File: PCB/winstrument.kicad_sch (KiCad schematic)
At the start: 94 parts, among them J1 Conn_01x05_Pin, J2 ICSP, J3 RS422, J4 Conn_01x08_Pin, J5 Conn_02x04_Odd_Even, J6 Conn_01x03_Pin, J7 Conn_01x02_Pin, Q1 2N7002, Q2 2N7002, Q3 2N7002, U1 STM32L432KCUx, U10 TLV9061xDBV, U11 TCMT1100, U12 TCMT1100, U2 TCAN337, U3 TPS5430DDA, U4 ADM3488ExR, U5 TLV75533PDBV, U6 NCP662SQ50, U7 TXB0104D, U8 TLV9061xDBV, U9 TPS27SA08CPWPR

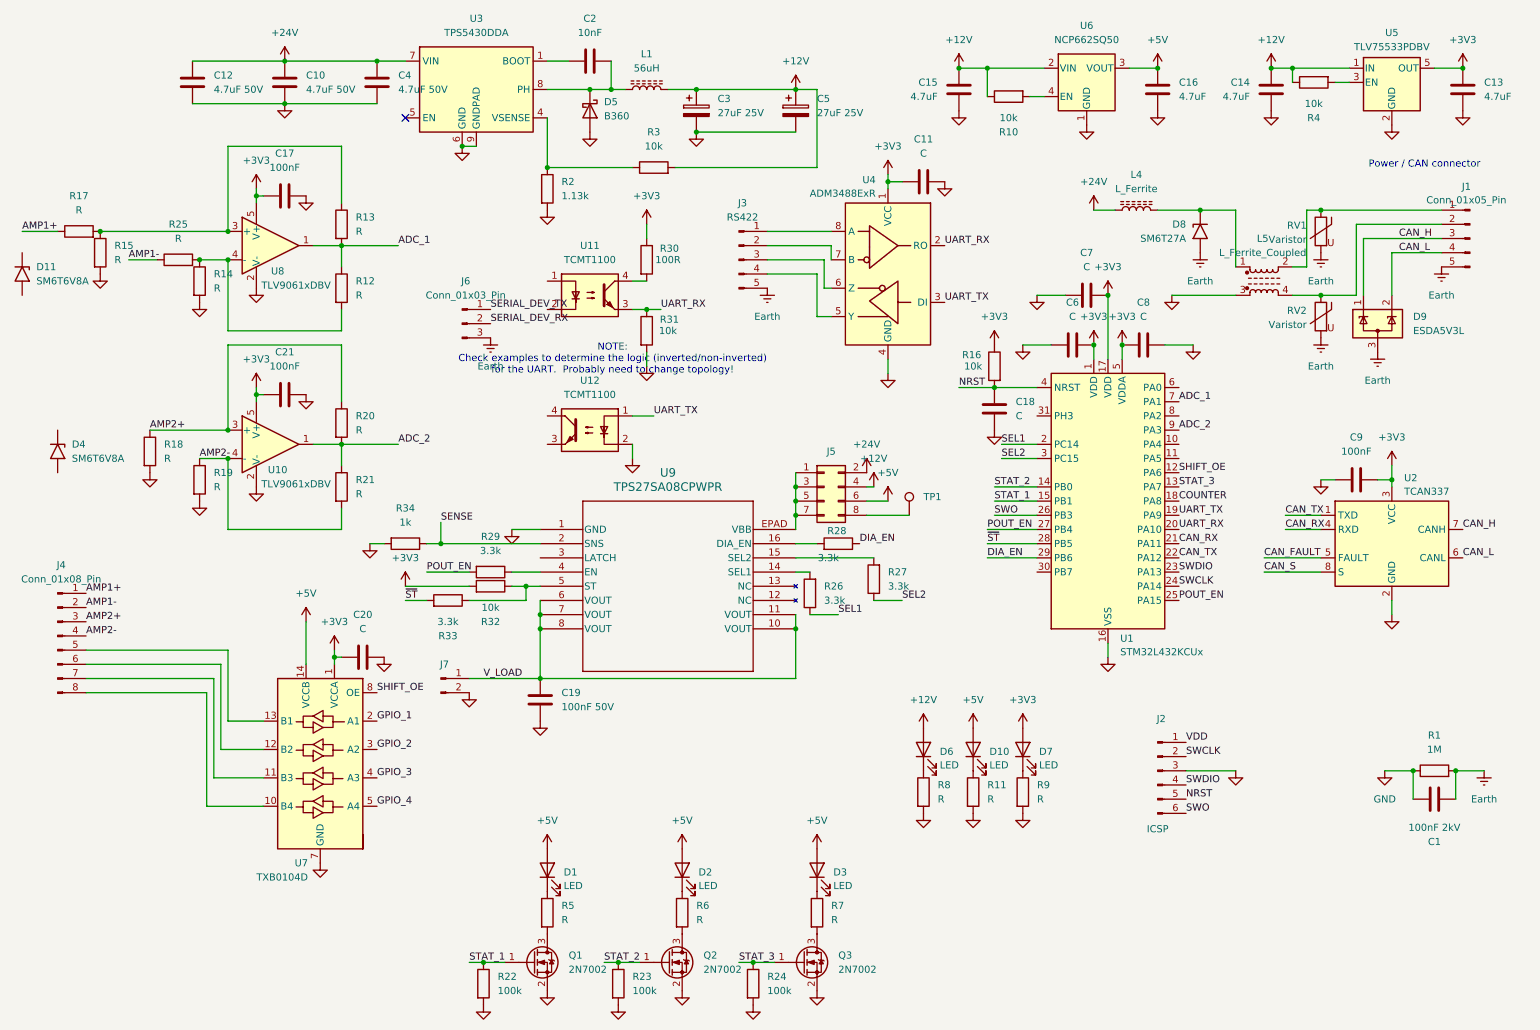
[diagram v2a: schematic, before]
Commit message: schematic capture and part specification mostly complete.  Still some uncertainty on the power common mode filter choke, could possibly go with a through-hole part on a toroid.  At least one footprint that requires creating or correcting, otherwise PCB is started.  No enclosure specified yet.
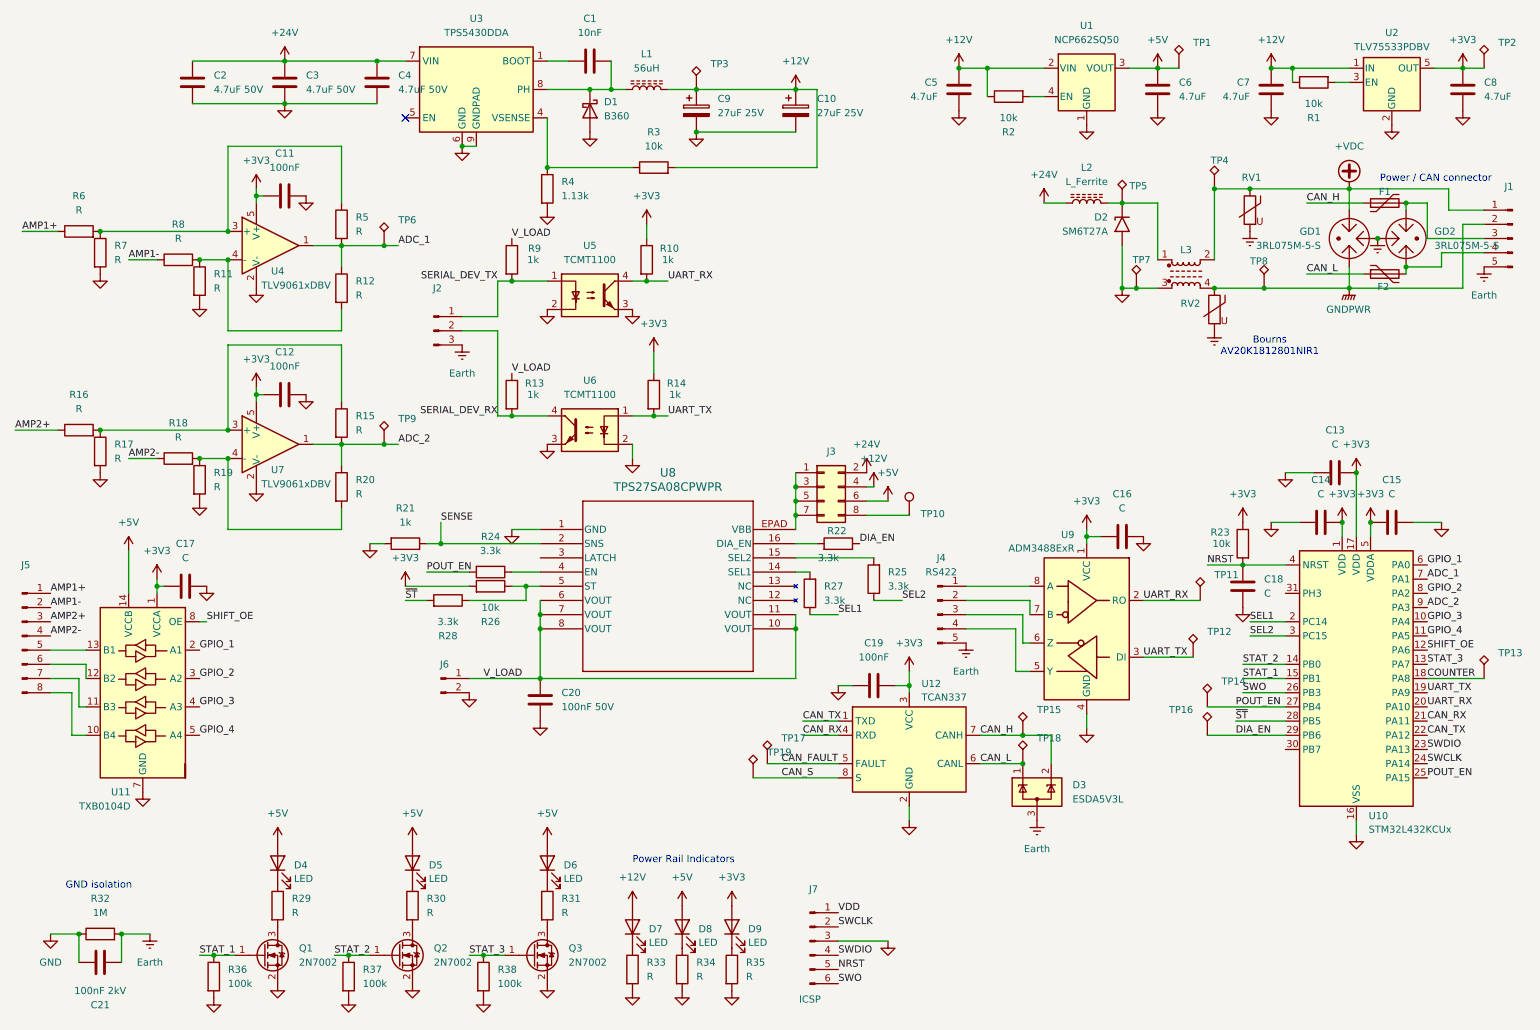
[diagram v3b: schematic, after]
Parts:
- removed D11, D4: SM6T6V8A, Diode_SMD:D_SMB, symbol Diode:SM6T6V8A
- removed J6: Conn_01x03_Pin, symbol Connector:Conn_01x03_Pin
- removed R31: 10k, symbol Device:R
- added F1, F2: TBU-CA-025-200-WH, Fuse:Fuse_Bourns_TBU-CA, symbol Power_Protection:TBU-CA-025-200-WH
- added GD1, GD2: 3RL075M-5-S, footprints:3R-5-S, symbol Device:GDT_3Pin
- added J2: Conn_01x03_Pin, Connector_Molex:Molex_KK-254_AE-6410-03A_1x03_P2.54mm_Vertical, symbol Connector:Conn_01x03_Pin
- added R13, R14, R9: 1k, Resistor_SMD:R_0603_1608Metric_Pad0.98x0.95mm_HandSolder, symbol Device:R
- added R16, R18: R, Resistor_SMD:R_0603_1608Metric_Pad0.98x0.95mm_HandSolder, symbol Device:R
- added TP1, TP11, TP12, TP13, TP14, TP15, TP16, TP17, TP18, TP19, TP2, TP3, TP4, TP5, TP6, TP7, TP8, TP9: TestPoint_Alt, TestPoint:TestPoint_Keystone_5019_Minature, symbol Connector:TestPoint_Alt
- C1: renamed from C2; footprint (none) -> Capacitor_SMD:C_0603_1608Metric_Pad1.08x0.95mm_HandSolder
- C10: renamed from C5; footprint (none) -> Capacitor_SMD:C_1808_4520Metric
- C11: renamed from C17; footprint (none) -> Capacitor_SMD:C_0603_1608Metric_Pad1.08x0.95mm_HandSolder
- C12: renamed from C21; footprint (none) -> Capacitor_SMD:C_0603_1608Metric_Pad1.08x0.95mm_HandSolder
- C13: renamed from C7; footprint (none) -> Capacitor_SMD:C_0603_1608Metric_Pad1.08x0.95mm_HandSolder
- C14: renamed from C6; footprint (none) -> Capacitor_SMD:C_0603_1608Metric_Pad1.08x0.95mm_HandSolder
- C15: renamed from C8; footprint (none) -> Capacitor_SMD:C_0603_1608Metric_Pad1.08x0.95mm_HandSolder
- C16: renamed from C11; footprint (none) -> Capacitor_SMD:C_0603_1608Metric_Pad1.08x0.95mm_HandSolder
- C17: renamed from C20; footprint (none) -> Capacitor_SMD:C_0603_1608Metric_Pad1.08x0.95mm_HandSolder
- C18: footprint (none) -> Capacitor_SMD:C_0603_1608Metric_Pad1.08x0.95mm_HandSolder
- C19: renamed from C9; footprint (none) -> Capacitor_SMD:C_0603_1608Metric_Pad1.08x0.95mm_HandSolder
- C2: renamed from C12; footprint (none) -> Capacitor_SMD:C_0805_2012Metric_Pad1.18x1.45mm_HandSolder; Manufacturer (none) -> Murata; Part Number (none) -> GRM21BR61H475KE51L
- C20: renamed from C19; footprint (none) -> Capacitor_SMD:C_0805_2012Metric
- C3: renamed from C10; footprint (none) -> Capacitor_SMD:C_0805_2012Metric_Pad1.18x1.45mm_HandSolder
- C4: footprint (none) -> Capacitor_SMD:C_0805_2012Metric_Pad1.18x1.45mm_HandSolder
- C5: renamed from C15; footprint (none) -> Capacitor_SMD:C_0805_2012Metric_Pad1.18x1.45mm_HandSolder
- C6: renamed from C16; footprint (none) -> Capacitor_SMD:C_0805_2012Metric_Pad1.18x1.45mm_HandSolder
- C7: renamed from C14; footprint (none) -> Capacitor_SMD:C_0805_2012Metric_Pad1.18x1.45mm_HandSolder
- C8: renamed from C13; footprint (none) -> Capacitor_SMD:C_0805_2012Metric_Pad1.18x1.45mm_HandSolder
- C9: renamed from C3; footprint (none) -> Capacitor_SMD:C_1808_4520Metric
- D4: renamed from D1; footprint (none) -> LED_SMD:LED_0603_1608Metric_Pad1.05x0.95mm_HandSolder
- D5: renamed from D2; footprint (none) -> LED_SMD:LED_0603_1608Metric_Pad1.05x0.95mm_HandSolder
- D6: renamed from D3; footprint (none) -> LED_SMD:LED_0603_1608Metric_Pad1.05x0.95mm_HandSolder
- D7: renamed from D6; footprint (none) -> LED_SMD:LED_0603_1608Metric_Pad1.05x0.95mm_HandSolder
- D8: renamed from D10; footprint (none) -> LED_SMD:LED_0603_1608Metric_Pad1.05x0.95mm_HandSolder
- D9: renamed from D7; footprint (none) -> LED_SMD:LED_0603_1608Metric_Pad1.05x0.95mm_HandSolder
- J1: footprint (none) -> Connector_Molex:Molex_KK-254_AE-6410-05A_1x05_P2.54mm_Vertical
- J3: renamed from J5; footprint (none) -> Connector_PinHeader_1.27mm:PinHeader_2x04_P1.27mm_Vertical
- J4: renamed from J3; footprint (none) -> Connector_Molex:Molex_KK-254_AE-6410-05A_1x05_P2.54mm_Vertical
- J5: renamed from J4; footprint (none) -> Connector_Molex:Molex_KK-254_AE-6410-08A_1x08_P2.54mm_Vertical
- J6: renamed from J7; footprint (none) -> Connector_Molex:Molex_KK-254_AE-6410-02A_1x02_P2.54mm_Vertical
- J7: renamed from J2; footprint (none) -> Connector_PinHeader_1.27mm:PinHeader_1x06_P1.27mm_Vertical
- L1: footprint (none) -> Inductor_SMD:L_Coilcraft_MSS1278H-XXX
- L2: renamed from L4; footprint (none) -> Inductor_SMD:L_0805_2012Metric_Pad1.05x1.20mm_HandSolder
- R1: renamed from R4; footprint (none) -> Resistor_SMD:R_0603_1608Metric_Pad0.98x0.95mm_HandSolder
- R10: renamed from R30; value 100R -> 1k; footprint (none) -> Resistor_SMD:R_0603_1608Metric_Pad0.98x0.95mm_HandSolder
- R11: renamed from R14; footprint (none) -> Resistor_SMD:R_0603_1608Metric_Pad0.98x0.95mm_HandSolder
- R12, R19, R3: footprint (none) -> Resistor_SMD:R_0603_1608Metric_Pad0.98x0.95mm_HandSolder
- R15: renamed from R20; footprint (none) -> Resistor_SMD:R_0603_1608Metric_Pad0.98x0.95mm_HandSolder
- R17: renamed from R18; footprint (none) -> Resistor_SMD:R_0603_1608Metric_Pad0.98x0.95mm_HandSolder
- R2: renamed from R10; footprint (none) -> Resistor_SMD:R_0603_1608Metric_Pad0.98x0.95mm_HandSolder
- R20: renamed from R21; footprint (none) -> Resistor_SMD:R_0603_1608Metric_Pad0.98x0.95mm_HandSolder
- R21: renamed from R34; footprint (none) -> Resistor_SMD:R_0603_1608Metric_Pad0.98x0.95mm_HandSolder
- R22: renamed from R28; footprint (none) -> Resistor_SMD:R_0603_1608Metric_Pad0.98x0.95mm_HandSolder
- R23: renamed from R16; footprint (none) -> Resistor_SMD:R_0603_1608Metric_Pad0.98x0.95mm_HandSolder
- R24: renamed from R29; footprint (none) -> Resistor_SMD:R_0603_1608Metric_Pad0.98x0.95mm_HandSolder
- R25: renamed from R27; footprint (none) -> Resistor_SMD:R_0603_1608Metric_Pad0.98x0.95mm_HandSolder
- R26: renamed from R32; footprint (none) -> Resistor_SMD:R_0603_1608Metric_Pad0.98x0.95mm_HandSolder
- R27: renamed from R26; footprint (none) -> Resistor_SMD:R_0603_1608Metric_Pad0.98x0.95mm_HandSolder
- R28: renamed from R33; footprint (none) -> Resistor_SMD:R_0603_1608Metric_Pad0.98x0.95mm_HandSolder
- R29: renamed from R5; footprint (none) -> Resistor_SMD:R_0603_1608Metric_Pad0.98x0.95mm_HandSolder
- R30: renamed from R6; footprint (none) -> Resistor_SMD:R_0603_1608Metric_Pad0.98x0.95mm_HandSolder
- R31: renamed from R7; footprint (none) -> Resistor_SMD:R_0603_1608Metric_Pad0.98x0.95mm_HandSolder
- R33: renamed from R8; footprint (none) -> Resistor_SMD:R_0603_1608Metric_Pad0.98x0.95mm_HandSolder
- R34: renamed from R11; footprint (none) -> Resistor_SMD:R_0603_1608Metric_Pad0.98x0.95mm_HandSolder
- R35: renamed from R9; footprint (none) -> Resistor_SMD:R_0603_1608Metric_Pad0.98x0.95mm_HandSolder
- R36: renamed from R22; footprint (none) -> Resistor_SMD:R_0603_1608Metric_Pad0.98x0.95mm_HandSolder
- R37: renamed from R23; footprint (none) -> Resistor_SMD:R_0603_1608Metric_Pad0.98x0.95mm_HandSolder
- R38: renamed from R24; footprint (none) -> Resistor_SMD:R_0603_1608Metric_Pad0.98x0.95mm_HandSolder
- R4: renamed from R2; footprint (none) -> Resistor_SMD:R_0603_1608Metric_Pad0.98x0.95mm_HandSolder
- R5: renamed from R13; footprint (none) -> Resistor_SMD:R_0603_1608Metric_Pad0.98x0.95mm_HandSolder
- R6: renamed from R17; footprint (none) -> Resistor_SMD:R_0603_1608Metric_Pad0.98x0.95mm_HandSolder
- R7: renamed from R15; footprint (none) -> Resistor_SMD:R_0603_1608Metric_Pad0.98x0.95mm_HandSolder
- R8: renamed from R25; footprint (none) -> Resistor_SMD:R_0603_1608Metric_Pad0.98x0.95mm_HandSolder
- RV1, RV2: footprint (none) -> Resistor_SMD:R_1812_4532Metric_Pad1.30x3.40mm_HandSolder
- TP10: renamed from TP1; footprint (none) -> TestPoint:TestPoint_Keystone_5019_Minature
- U12: renamed from U2; footprint (none) -> Package_SO:SOIC-8-1EP_3.9x4.9mm_P1.27mm_EP2.29x3mm
- U8: renamed from U9; footprint TSSOP_CPWPR_TEX -> footprints:TSSOP_CPWPR_TEX
- renumbered C1 to C21, D5 to D1, D8 to D2, D9 to D3, L5 to L3, R1 to R32, U6 to U1, U1 to U10, U7 to U11, U5 to U2, U8 to U4, U11 to U5, U12 to U6, U10 to U7, U4 to U9
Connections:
- net +12V: now also TP3.1
- net +3V3: now also R14.1, TP2.1
- net +5V: now also TP1.1
- net ADC_1: now also TP6.1
- net ADC_2: now also TP9.1
- net AMP2+: now also R16.1; no longer R15.1, R17.1, U7.3 (+)
- net AMP2-: now also R18.1; no longer R19.1, R20.2, U7.4 (-)
- net CAN_FAULT: now also TP17.1
- net CAN_H: now also D3.2 (K), F1.1, TP15.1; no longer D3.1 (K), J1.3 (Pin_3)
- net CAN_L: now also D3.1 (K), F2.1, TP18.1; no longer D3.2 (K), J1.4 (Pin_4)
- net CAN_S: now also TP19.1
- net COUNTER: now also TP13.1
- net DIA_EN: now also TP16.1
- net Earth: now also GD1.2, GD2.2, J2.3 (Pin_3); no longer D2.2 (A2)
- net GND: now also D2.2 (A2), U5.2, U5.3, U6.3, TP7.1
- net GPIO_1: now also U10.6 (PA0)
- net GPIO_2: now also U10.8 (PA2)
- net GPIO_3: now also U10.10 (PA4)
- net GPIO_4: now also U10.11 (PA5)
- net POUT_EN: now also TP14.1
- net SERIAL_DEV_RX: now also U6.4, J2.2 (Pin_2), R13.2
- net SERIAL_DEV_TX: now also U5.1, J2.1 (Pin_1), R9.2
- net UART_RX: now also R10.2, U5.4, TP11.1; no longer U5.3
- net UART_TX: now also R14.2, TP12.1
- net V_LOAD: now also R13.1, R9.1
- net GNDPWR: now reaches J1.2 (Pin_2), L3.4, RV2.1
- net GNDPWR: now also GD1.1, TP8.1
- net at D2.1 (A1), L2.2, L3.1: now also TP5.1
- net +VDC: now reaches J1.1 (Pin_1), L3.2, RV1.1
- net +VDC: now also GD1.3, TP4.1
- new net: F2.3, GD2.1, J1.4 (Pin_4)
- new net: F1.3, GD2.3, J1.3 (Pin_3)
- new net: R15.1, R16.2, R17.1, U7.3 (+)
- new net: R18.2, R19.1, R20.2, U7.4 (-)
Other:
- note added: "Bourns AV20K1812801NIR1"
- note added: "GND isolation"
- note added: "Power Rail Indicators"
- note removed: "NOTE: Check examples to determine the logic (inverted/non-inverted) for the UART. Probably need to change topology!"
- moved on the sheet: C13, C14, C15, C16, C17, C18, C19, C21, D2, D3, D4, D5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

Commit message: commit to catch up the repo to changes in PCB design
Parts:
- TP1, TP10, TP11, TP12, TP13, TP15, TP16, TP17, TP18, TP19, TP2, TP3, TP4, TP5, TP6, TP7, TP8, TP9: footprint TestPoint:TestPoint_Keystone_5019_Minature -> TestPoint:TestPoint_Keystone_5015_Micro-Minature
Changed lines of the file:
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@@
 			)
 		)
-		(property "Footprint" "TestPoint:TestPoint_Keystone_5019_Minature"
+		(property "Footprint" "TestPoint:TestPoint_Keystone_5015_Micro-Minature"
 			(at 228.6 25.4 0)
 			(effects
@@
 			)
 		)
-		(property "Footprint" "TestPoint:TestPoint_Keystone_5019_Minature"
+		(property "Footprint" "TestPoint:TestPoint_Keystone_5015_Micro-Minature"
 			(at 283.21 134.62 0)
 			(effects
@@
 			)
 		)
-		(property "Footprint" "TestPoint:TestPoint_Keystone_5019_Minature"
+		(property "Footprint" "TestPoint:TestPoint_Keystone_5015_Micro-Minature"
 			(at 232.41 120.65 0)
 			(effects
@@
 			)
 		)
-		(property "Footprint" "TestPoint:TestPoint_Keystone_5019_Minature"
+		(property "Footprint" "TestPoint:TestPoint_Keystone_5015_Micro-Minature"
 			(at 200.66 144.78 0)
 			(effects
@@
 			)
 		)
-		(property "Footprint" "TestPoint:TestPoint_Keystone_5019_Minature"
+		(property "Footprint" "TestPoint:TestPoint_Keystone_5015_Micro-Minature"
 			(at 154.94 149.86 0)
 			(effects
@@
 			)
 		)
-		(property "Footprint" "TestPoint:TestPoint_Keystone_5019_Minature"
+		(property "Footprint" "TestPoint:TestPoint_Keystone_5015_Micro-Minature"
 			(at 231.14 130.81 0)
 			(effects
@@
 			)
 		)
-		(property "Footprint" "TestPoint:TestPoint_Keystone_5019_Minature"
+		(property "Footprint" "TestPoint:TestPoint_Keystone_5015_Micro-Minature"
 			(at 152.4 152.4 0)
 			(effects
@@
 			)
 		)
-		(property "Footprint" "TestPoint:TestPoint_Keystone_5019_Minature"
+		(property "Footprint" "TestPoint:TestPoint_Keystone_5015_Micro-Minature"
 			(at 223.52 144.78 0)
 			(effects
@@
 			)
 		)
-		(property "Footprint" "TestPoint:TestPoint_Keystone_5019_Minature"
+		(property "Footprint" "TestPoint:TestPoint_Keystone_5015_Micro-Minature"
 			(at 218.44 49.53 0)
 			(effects
@@
 			)
 		)
-		(property "Footprint" "TestPoint:TestPoint_Keystone_5019_Minature"
+		(property "Footprint" "TestPoint:TestPoint_Keystone_5015_Micro-Minature"
 			(at 243.84 64.77 0)
 			(effects
@@
 			)
 		)
-		(property "Footprint" "TestPoint:TestPoint_Keystone_5019_Minature"
+		(property "Footprint" "TestPoint:TestPoint_Keystone_5015_Micro-Minature"
 			(at 86.36 92.71 0)
 			(effects
@@
 			)
 		)
-		(property "Footprint" "TestPoint:TestPoint_Keystone_5019_Minature"
+		(property "Footprint" "TestPoint:TestPoint_Keystone_5015_Micro-Minature"
 			(at 283.21 25.4 0)
 			(effects
@@
 			)
 		)
-		(property "Footprint" "TestPoint:TestPoint_Keystone_5019_Minature"
+		(property "Footprint" "TestPoint:TestPoint_Keystone_5015_Micro-Minature"
 			(at 142.24 29.21 0)
 			(effects
@@
 			)
 		)
-		(property "Footprint" "TestPoint:TestPoint_Keystone_5019_Minature"
+		(property "Footprint" "TestPoint:TestPoint_Keystone_5015_Micro-Minature"
 			(at 210.82 64.77 0)
 			(effects
@@
 			)
 		)
-		(property "Footprint" "TestPoint:TestPoint_Keystone_5019_Minature"
+		(property "Footprint" "TestPoint:TestPoint_Keystone_5015_Micro-Minature"
 			(at 224.79 46.99 0)
 			(effects
@@
 			)
 		)
-		(property "Footprint" "TestPoint:TestPoint_Keystone_5019_Minature"
+		(property "Footprint" "TestPoint:TestPoint_Keystone_5015_Micro-Minature"
 			(at 86.36 57.15 0)
 			(effects
@@
 			)
 		)
-		(property "Footprint" "TestPoint:TestPoint_Keystone_5019_Minature"
+		(property "Footprint" "TestPoint:TestPoint_Keystone_5015_Micro-Minature"
 			(at 200.66 149.86 0)
 			(effects
@@
 			)
 		)
-		(property "Footprint" "TestPoint:TestPoint_Keystone_5019_Minature"
+		(property "Footprint" "TestPoint:TestPoint_Keystone_5015_Micro-Minature"
 			(at 180.34 105.41 0)
 			(effects

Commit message: modified schematics to replace parts and redesign serial interfaces.  Replaced general purpose opamps with adjustable gain instrumentation amplifiers that are more appropriate.
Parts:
- removed D6: LED, LED_SMD:LED_0603_1608Metric_Pad1.05x0.95mm_HandSolder, symbol Device:LED
- removed J5: Conn_01x08_Pin, Connector_Molex:Molex_KK-254_AE-6410-08A_1x08_P2.54mm_Vertical, symbol Connector:Conn_01x08_Pin
- removed Q3: 2N7002, Package_TO_SOT_SMD:SOT-23, symbol Transistor_FET:2N7002
- removed R10, R13, R14, R9: 1k, Resistor_SMD:R_0603_1608Metric_Pad0.98x0.95mm_HandSolder, symbol Device:R
- removed R20, R31: R, Resistor_SMD:R_0603_1608Metric_Pad0.98x0.95mm_HandSolder, symbol Device:R
- removed R38: 100k, Resistor_SMD:R_0603_1608Metric_Pad0.98x0.95mm_HandSolder, symbol Device:R
- removed U4, U7: TLV9061xDBV, Package_TO_SOT_SMD:SOT-23-5, symbol Amplifier_Operational:TLV9061xDBV
- removed U5, U6: TCMT1100, Package_SO:SOP-4_4.4x2.6mm_P1.27mm, symbol Isolator:TCMT1100
- added C22, C23, C24, C25, C26: C, symbol Device:C
- added J5: Conn_01x09_Pin, Connector_Molex:Molex_KK-254_AE-6410-09A_1x09_P2.54mm_Vertical, symbol Connector:Conn_01x09_Pin
- added U13, U14: INA326, Package_SO:MSOP-8_3x3mm_P0.65mm, symbol Amplifier_Instrumentation:INA326
- added U7: ST232ExD, Package_SO:SOIC-16_3.9x9.9mm_P1.27mm, symbol Interface_UART:ST232ExD
- C11: value 100nF -> C
- C12: value 100nF -> C; footprint Capacitor_SMD:C_0603_1608Metric_Pad1.08x0.95mm_HandSolder -> (none)
- L3: value L_Ferrite_Coupled -> MSD1278-105; footprint (none) -> CoilcraftPCB:MSD1278 SERIES
- R11, R12, R16, R17, R18, R19, R5, R6, R7, R8: footprint Resistor_SMD:R_0603_1608Metric_Pad0.98x0.95mm_HandSolder -> (none)
- R15: value R -> 0R; footprint Resistor_SMD:R_0603_1608Metric_Pad0.98x0.95mm_HandSolder -> Resistor_SMD:R_1206_3216Metric; now not fitted
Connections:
- net STAT_3 is gone; now on net CAN_FAULT: U10.13 (PA7)
- net +3V3: now also C26.1, U13.7 (V+), U14.7 (V+); no longer C11.1, C17.1, U11.1 (VCCA)
- net +5V: no longer U11.14 (VCCB)
- net ADC_1: now also R19.2, C25.2; no longer R12.1, R5.2
- net ADC_2: now also R18.2, C24.2; no longer R15.2
- net AMP1+: now also R12.1, U14.3 (+); no longer R6.1
- net AMP1-: now also U14.2 (-)
- net AMP2+: now also R11.1, U13.3 (+); no longer R16.1
- net AMP2-: now also R7.1, U13.2 (-); no longer R18.1
- net Earth: now also R15.1, J5.9 (Pin_9)
- net GND: now also C11.1, R12.2, R16.2, R8.2, C22.1, C23.1, C24.1, C25.1, C26.2, U13.4 (V-), U14.4 (V-); no longer C11.2, R19.2
- net GNDPWR: now also R15.2
- net GPIO_1: no longer U11.2 (A1)
- net GPIO_2: no longer U11.3 (A2)
- net GPIO_3: no longer U11.4 (A3)
- net GPIO_4: no longer U11.5 (A4)
- net SEL1: no longer R27.1
- net SERIAL_DEV_RX: no longer J2.2 (Pin_2)
- net SERIAL_DEV_TX: no longer J2.1 (Pin_1)
- net SHIFT_OE: no longer U11.8 (OE)
- net at R19.1: now also U14.6; no longer R18.2
- new net: C23.2, R17.1, U14.5 (R2)
- new net: R5.1, U13.1 (R1)
- new net: C22.2, R16.1, U13.5 (R2)
- new net: R18.1, U13.6
- new net: R5.2, U13.8 (R1)
- new net: R6.1, U14.1 (R1)
- new net: R6.2, U14.8 (R1)
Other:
- note added: "Isat 1.1A"
- note added: "Load SW for Instrument"
- note added: "Screen"
- note added: "TODO: Revisit if TPS27 is configured/pinned to uC correctly"
- title: (none) -> Geophysical Instrument Common Interface
- moved on the sheet: C17, C19, C21, D3, D4, D5, J2, J4, J7, Q1, Q2, R29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

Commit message: replaced microcontroller due to requirements for more interface pins and additional capabilities in processing power and memory that would improve performance in signal processing
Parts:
- removed C13, C14, C15, C18: C, Capacitor_SMD:C_0603_1608Metric_Pad1.08x0.95mm_HandSolder, symbol Device:C
- removed R23: 10k, Resistor_SMD:R_0603_1608Metric_Pad0.98x0.95mm_HandSolder, symbol Device:R
- removed TP13, TP16: TestPoint_Alt, TestPoint:TestPoint_Keystone_5015_Micro-Minature, symbol Connector:TestPoint_Alt
- removed TP14: TestPoint_Alt, TestPoint:TestPoint_Keystone_5019_Minature, symbol Connector:TestPoint_Alt
- removed U10: STM32L432KCUx, Package_DFN_QFN:QFN-32-1EP_5x5mm_P0.5mm_EP3.45x3.45mm, symbol MCU_ST_STM32L4:STM32L432KCUx
- added U4: STM32L552CETx, Package_QFP:LQFP-48_7x7mm_P0.5mm, symbol MCU_ST_STM32L5:STM32L552CETx
- L3: value MSD1278-105 -> MSD1514T-473MED; footprint CoilcraftPCB:MSD1278 SERIES -> CoilcraftPCB:MSD1583 SERIES
- R18, R19: value R -> 100R
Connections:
- net VDD: no longer names the net of J7.1 (Pin_1)
- new net: U4.23 (VSS), U4.35 (VSS), U4.47 (VSS)
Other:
- note added: "GND isolation (may be optional?)"
- note added: "Irms 3A"
- note removed: "GND isolation"
- note removed: "Isat 1.1A"
- moved on the sheet: C16, J4, J7, TP11, TP12, U9
